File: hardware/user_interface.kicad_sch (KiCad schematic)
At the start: 0 parts

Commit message: Completed the Oled display and breakout for remaining pins
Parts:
- added J4: Conn_01x04_Pin, symbol Connector:Conn_01x04_Pin
- added J5: Conn_01x05_Pin, symbol Connector:Conn_01x05_Pin
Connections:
- new net +3.3V: J4.1 (Pin_1), J5.1 (Pin_1)
- new net GND: J4.4 (Pin_4), J5.5 (Pin_5)
- new net GPIO18: J5.3 (Pin_3)
- new net GPIO19: J5.4 (Pin_4)
- new net GPIO8: J5.2 (Pin_2)
- new net SCL: J4.3 (Pin_3)
- new net SDA: J4.2 (Pin_2)

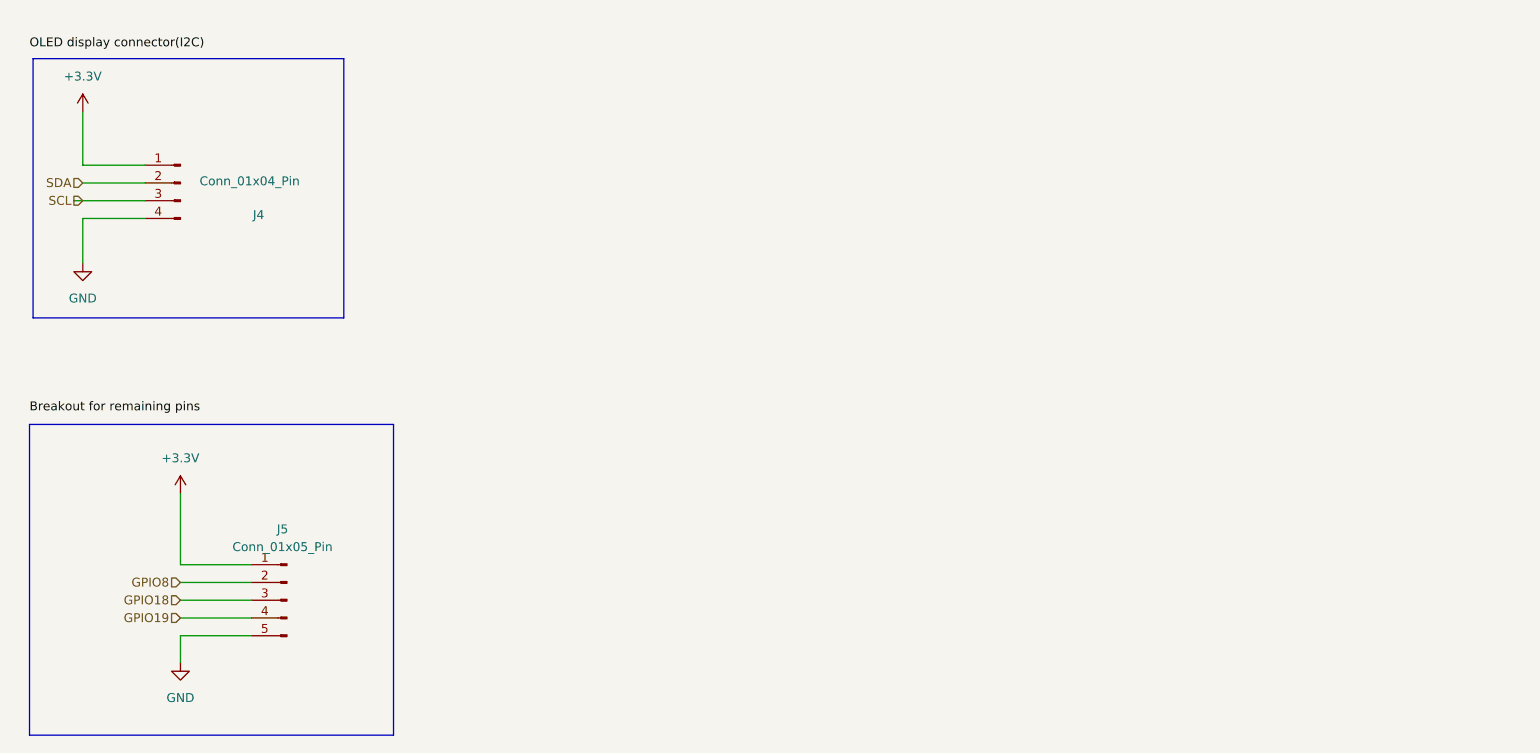
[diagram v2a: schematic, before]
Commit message: Completed the user interface
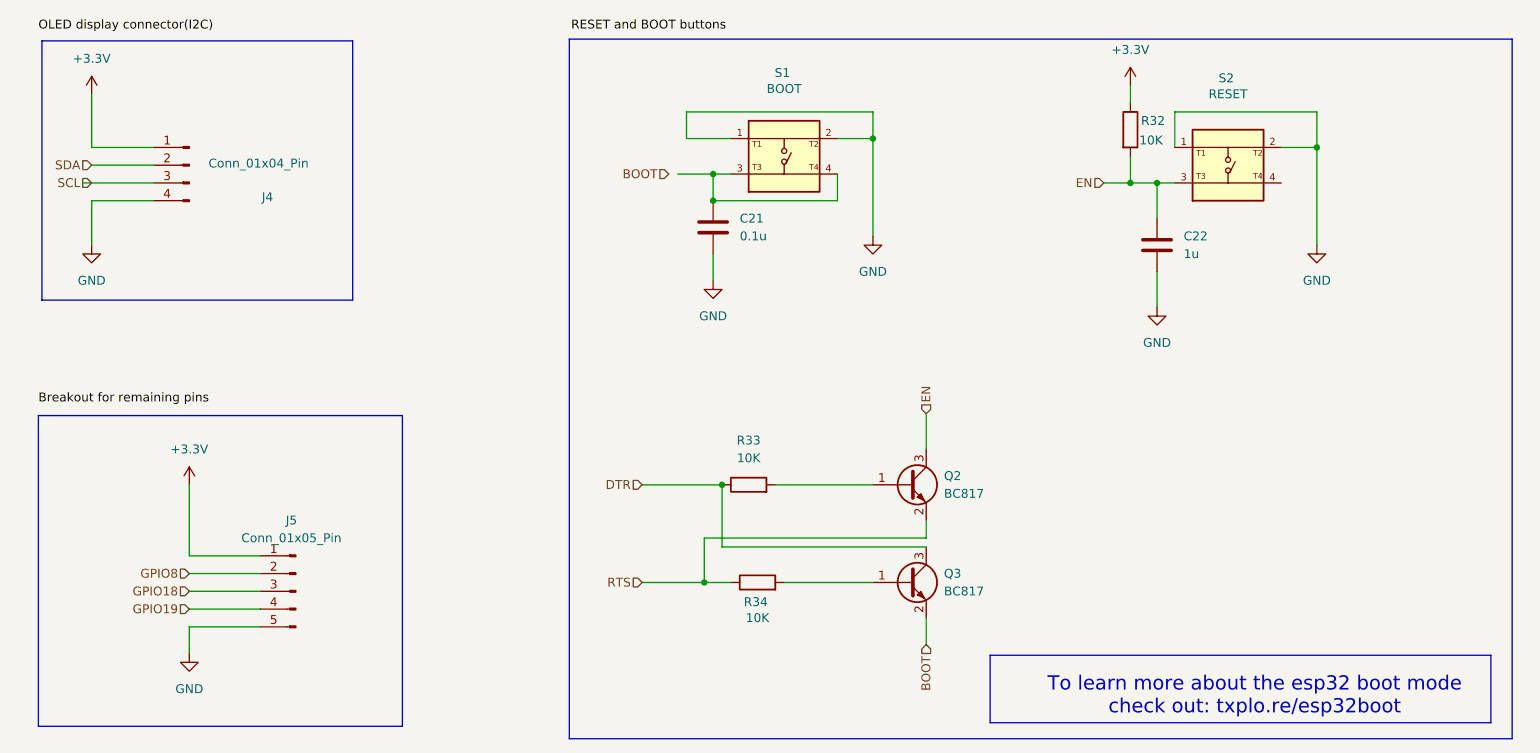
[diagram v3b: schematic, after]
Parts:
- added C21: 0.1u, symbol Device:C
- added C22: 1u, symbol Device:C
- added Q2, Q3: BC817, Package_TO_SOT_SMD:SOT-23, symbol Transistor_BJT:BC817
- added R32, R33, R34: 10K, symbol Device:R
- added S1: BOOT, USLPT2819DT2TR:SW_USLPT2819DT2TR, symbol USLPT2819DT2TR:USLPT2819DT2TR
- added S2: RESET, USLPT2819DT2TR:SW_USLPT2819DT2TR, symbol USLPT2819DT2TR:USLPT2819DT2TR
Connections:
- net +3.3V: now also R32.1
- net GND: now also C21.2, C22.2, S1.1, S1.2, S2.1, S2.2
- new net: Q3.1 (B), R34.2
- new net: Q2.1 (B), R33.2
- new net: C21.1, S1.3, S1.4
- new net BOOT: Q3.2 (E)
- new net DTR: Q3.3 (C), R33.1
- new net EN: C22.1, Q2.3 (C), R32.2, S2.3
- new net RTS: Q2.2 (E), R34.1
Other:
- note added: "To learn more about the esp32 boot mode check out: txplo.re/esp32boot"
- moved on the sheet: J4, J5

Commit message: Completed Assigning footprints and correcting some mistakes
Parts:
- C19: renamed from C21; footprint (none) -> Capacitor_SMD:C_0805_2012Metric
- C20: renamed from C22; footprint (none) -> Capacitor_SMD:C_0805_2012Metric
- J4: footprint (none) -> Connector_PinHeader_2.54mm:PinHeader_1x04_P2.54mm_Vertical
- J5: footprint (none) -> Connector_PinHeader_2.54mm:PinHeader_1x05_P2.54mm_Vertical
- R30: renamed from R33; footprint (none) -> Resistor_SMD:R_0805_2012Metric
- R31: renamed from R34; footprint (none) -> Resistor_SMD:R_0805_2012Metric
- R32: footprint (none) -> Resistor_SMD:R_0805_2012Metric
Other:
- note added: "Breakout for remaining pins"
- note added: "OLED display connector(I2C)"
- note added: "RESET and BOOT buttons"
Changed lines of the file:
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@@
+		)
+	)
+	(text "Breakout for remaining pins"
+		(exclude_from_sim no)
+		(at 66.548 77.978 0)
+		(effects
+			(font
+				(size 1.27 1.27)
+			)
+		)
+	)
+	(text "OLED display connector(I2C)"
+		(exclude_from_sim no)
+		(at 67.564 24.638 0)
+		(effects
+			(font
+				(size 1.27 1.27)
+			)
 		)
 	)
@@
 			(font
 				(size 2.032 2.032)
+			)
+		)
+	)
+	(text "RESET and BOOT buttons"
+		(exclude_from_sim no)
+		(at 141.224 24.384 0)
+		(effects
+			(font
+				(size 1.27 1.27)
 			)
 		)
@@
 		)
 	)
-	(label "OLED display connector(I2C)"
-		(at 53.34 25.4 0)
-		(effects
-			(font
-				(size 1.27 1.27)
-			)
-			(justify left bottom)
-		)
-	)
-	(label "RESET and BOOT buttons"
-		(at 129.54 25.4 0)
-		(effects
-			(font
-				(size 1.27 1.27)
-			)
-			(justify left bottom)
-		)
-	)
-	(label "Breakout for remaining pins"
-		(at 53.34 78.74 0)
-		(effects
-			(font
-				(size 1.27 1.27)
-			)
-			(justify left bottom)
-		)
-	)
 	(hierarchical_label "EN"
 		(shape input)
@@
 		(dnp no)
 		(fields_autoplaced yes)
-		(property "Reference" "R33"
+		(property "Reference" "R30"
 			(at 154.94 83.82 90)
 			(show_name no)
@@
 			)
 		)
-		(property "Footprint" ""
+		(property "Footprint" "Resistor_SMD:R_0805_2012Metric"
 			(at 154.94 91.948 90)
 			(hide yes)
@@
 			(project "iot_board"
 				(path "/32f4a40d-6939-405a-8e7e-c6d0e82e69e6/0016dce1-cab5-4d90-b9e5-1e0111bd767f/04348eb2-b538-4784-9d32-eae9f7adbede"
-					(reference "R33")
+					(reference "R30")
 					(unit 1)
 				)
@@
 			)
 		)
-		(property "Footprint" ""
+		(property "Footprint" "Connector_PinHeader_2.54mm:PinHeader_1x05_P2.54mm_Vertical"
 			(at 90.17 105.41 0)
 			(hide yes)
@@
 			)
 		)
-		(property "Footprint" ""
+		(property "Footprint" "Connector_PinHeader_2.54mm:PinHeader_1x04_P2.54mm_Vertical"
 			(at 74.93 44.45 0)
 			(hide yes)
@@
 		(dnp no)
 		(fields_autoplaced yes)
-		(property "Reference" "#PWR047"
+		(property "Reference" "#PWR048"
 			(at 60.96 62.23 0)
 			(hide yes)
@@
 			(project "iot_board"
 				(path "/32f4a40d-6939-405a-8e7e-c6d0e82e69e6/0016dce1-cab5-4d90-b9e5-1e0111bd767f/04348eb2-b538-4784-9d32-eae9f7adbede"
-					(reference "#PWR047")
+					(reference "#PWR048")
 					(unit 1)
 				)
@@
 		(dnp no)
 		(fields_autoplaced yes)
-		(property "Reference" "C21"
+		(property "Reference" "C19"
 			(at 153.67 52.0699 0)
 			(show_name no)
@@
 			)
 		)
-		(property "Footprint" ""
+		(property "Footprint" "Capacitor_SMD:C_0805_2012Metric"
 			(at 150.8252 57.15 0)
 			(hide yes)
@@
 			(project "iot_board"
 				(path "/32f4a40d-6939-405a-8e7e-c6d0e82e69e6/0016dce1-cab5-4d90-b9e5-1e0111bd767f/04348eb2-b538-4784-9d32-eae9f7adbede"
-					(reference "C21")
+					(reference "C19")
 					(unit 1)
 				)
@@
 		(dnp no)
 		(fields_autoplaced yes)
-		(property "Reference" "#PWR048"
+		(property "Reference" "#PWR047"
 			(at 60.96 38.1 0)
 			(hide yes)
@@
 			(project "iot_board"
 				(path "/32f4a40d-6939-405a-8e7e-c6d0e82e69e6/0016dce1-cab5-4d90-b9e5-1e0111bd767f/04348eb2-b538-4784-9d32-eae9f7adbede"
-					(reference "#PWR048")
+					(reference "#PWR047")
 					(unit 1)
 				)
@@
 		(dnp no)
 		(fields_autoplaced yes)
-		(property "Reference" "#PWR051"
+		(property "Reference" "#PWR052"
 			(at 172.72 60.96 0)
 			(hide yes)
@@
 			(project "iot_board"
 				(path "/32f4a40d-6939-405a-8e7e-c6d0e82e69e6/0016dce1-cab5-4d90-b9e5-1e0111bd767f/04348eb2-b538-4784-9d32-eae9f7adbede"
-					(reference "#PWR051")
+					(reference "#PWR052")
 					(unit 1)
 				)
@@
 		(dnp no)
 		(fields_autoplaced yes)
-		(property "Reference" "#PWR053"
+		(property "Reference" "#PWR055"
 			(at 236.22 62.23 0)
 			(hide yes)
@@
 			(project "iot_board"
 				(path "/32f4a40d-6939-405a-8e7e-c6d0e82e69e6/0016dce1-cab5-4d90-b9e5-1e0111bd767f/04348eb2-b538-4784-9d32-eae9f7adbede"
-					(reference "#PWR053")
+					(reference "#PWR055")
 					(unit 1)
 				)
@@
 			)
 		)
-		(property "Footprint" ""
+		(property "Footprint" "Resistor_SMD:R_0805_2012Metric"
 			(at 207.772 39.37 90)
 			(hide yes)
@@
 		(dnp no)
 		(fields_autoplaced yes)
-		(property "Reference" "#PWR055"
+		(property "Reference" "#PWR053"
 			(at 209.55 36.83 0)
 			(hide yes)
@@
 			(project "iot_board"
 				(path "/32f4a40d-6939-405a-8e7e-c6d0e82e69e6/0016dce1-cab5-4d90-b9e5-1e0111bd767f/04348eb2-b538-4784-9d32-eae9f7adbede"
-					(reference "#PWR055")
+					(reference "#PWR053")
 					(unit 1)
 				)
@@
 		(dnp no)
 		(fields_autoplaced yes)
-		(property "Reference" "#PWR052"
+		(property "Reference" "#PWR051"
 			(at 149.86 67.31 0)
 			(hide yes)
@@
 			(project "iot_board"
 				(path "/32f4a40d-6939-405a-8e7e-c6d0e82e69e6/0016dce1-cab5-4d90-b9e5-1e0111bd767f/04348eb2-b538-4784-9d32-eae9f7adbede"
-					(reference "#PWR052")
+					(reference "#PWR051")
 					(unit 1)
 				)
@@
 		(in_pos_files yes)
 		(dnp no)
-		(property "Reference" "R34"
+		(property "Reference" "R31"
 			(at 155.956 106.934 90)
 			(show_name no)
@@
 			)
 		)
-		(property "Footprint" ""
+		(property "Footprint" "Resistor_SMD:R_0805_2012Metric"
 			(at 156.21 105.918 90)
 			(hide yes)
@@
 			(project "iot_board"
 				(path "/32f4a40d-6939-405a-8e7e-c6d0e82e69e6/0016dce1-cab5-4d90-b9e5-1e0111bd767f/04348eb2-b538-4784-9d32-eae9f7adbede"
-					(reference "R34")
+					(reference "R31")
 					(unit 1)
 				)
@@
 		(dnp no)
 		(fields_autoplaced yes)
-		(property "Reference" "C22"
+		(property "Reference" "C20"
 			(at 217.17 54.6099 0)
 			(show_name no)
@@
 			)
 		)
-		(property "Footprint" ""
+		(property "Footprint" "Capacitor_SMD:C_0805_2012Metric"
 			(at 214.3252 59.69 0)
 			(hide yes)
@@
 			(project "iot_board"
 				(path "/32f4a40d-6939-405a-8e7e-c6d0e82e69e6/0016dce1-cab5-4d90-b9e5-1e0111bd767f/04348eb2-b538-4784-9d32-eae9f7adbede"
-					(reference "C22")
+					(reference "C20")
 					(unit 1)
 				)
